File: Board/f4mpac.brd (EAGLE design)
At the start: 59.7 x 82.5 mm, 53 parts, among them CN1 DIP40 MB CONN, IC1 YM2413, IC10 27C512AL, IC2 74LS30D, IC3 74LS04D, IC4 LM4558N, IC5 Z80, IC6 74LS30D, IC7 74LS02D, IC8 74LS74D, IC9 74LS125D

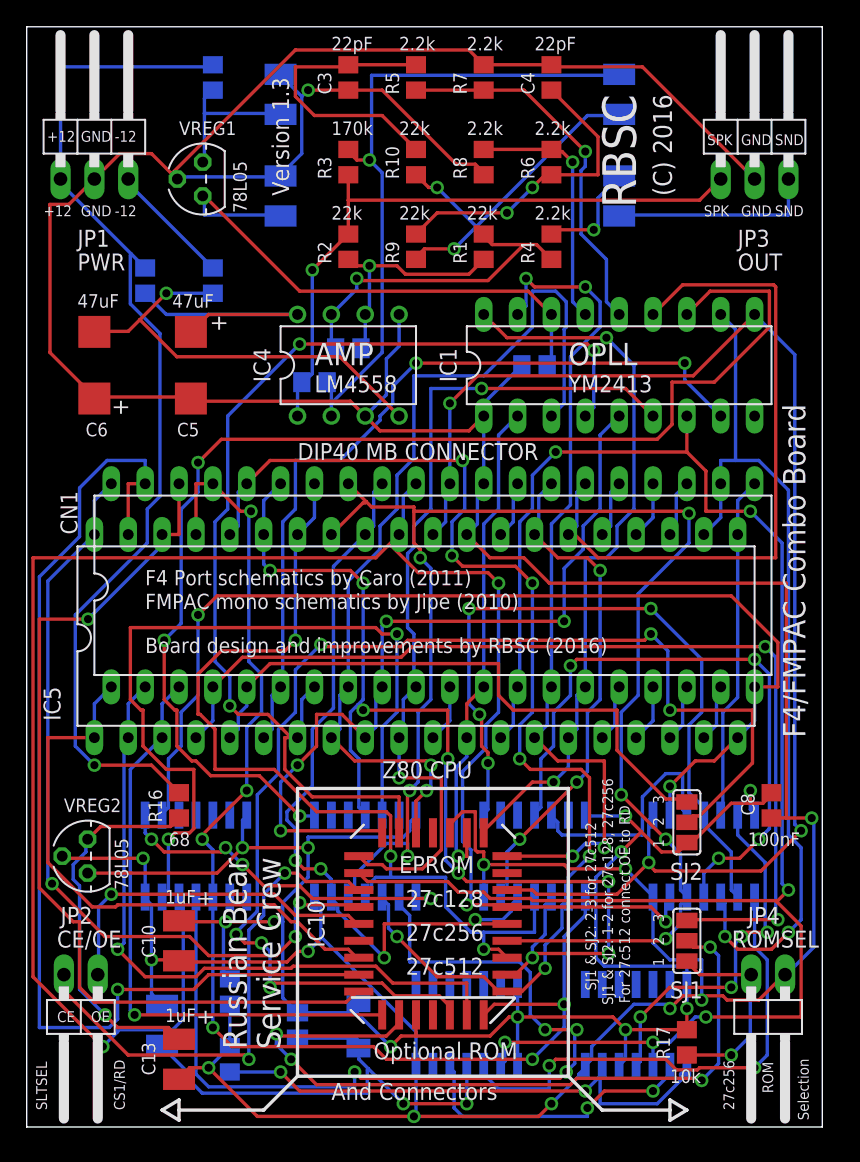
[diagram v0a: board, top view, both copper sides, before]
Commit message: Release 23.01.2019
Improved board, redrawn schematics
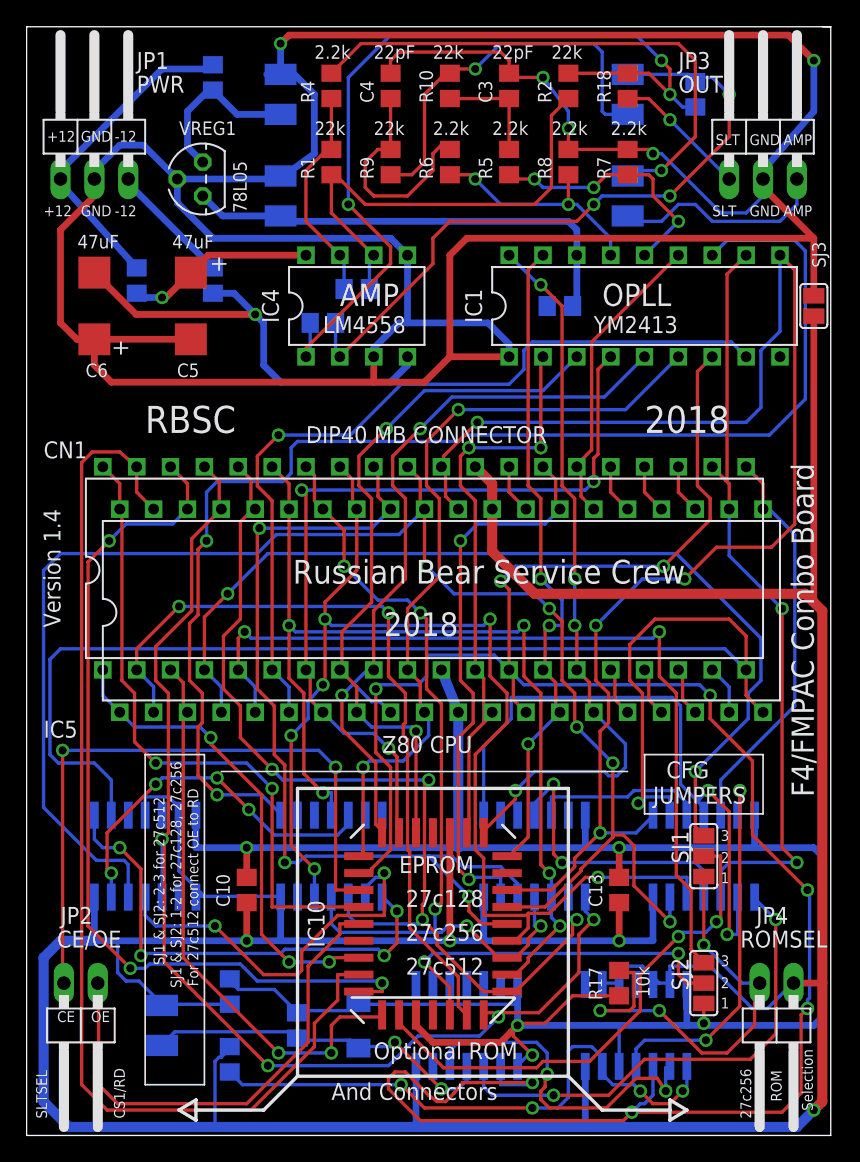
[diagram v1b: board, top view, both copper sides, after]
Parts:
- removed C15: 100nF, rcl:C0805
- removed R16: 68, rcl:R0805
- removed VREG2: 7805L, linear:TO92
- added R18: 1k, rcl:R0805
- added SJ3: (no value), jumper:SJ
- C10, C13: value 1uF 25v -> 100nF; device rcl:SMC_B -> rcl:C0805
- R4: value 2.2k -> 4.7k
- moved C8 40.7 mm to (40.0, 61.6), flipped to the bottom, turned to 180 degrees
- moved C13 35.4 mm to (44.5, 17.8)
- moved R3 26.5 mm to (50.2, 77.5), flipped to the bottom
- moved R2 20.4 mm to (40.6, 78.1)
- moved R4 20.4 mm to (22.9, 78.1)
- moved R1 13.1 mm to (22.9, 72.4)
- moved R7 12.5 mm to (45.1, 72.4)
- moved SJ2 12.1 mm to (50.8, 10.8)
- moved C3 12.1 mm to (36.2, 78.1), turned to 270 degrees
- moved C4 12.1 mm to (27.3, 78.1)
- moved R5 9.44 mm to (36.2, 72.4)
- moved R6 7.62 mm to (31.8, 72.4), turned to 90 degrees
- moved R17 6.75 mm to (44.5, 10.8), turned to 90 degrees
- moved R9 6.63 mm to (27.3, 72.4)
- moved SJ1 6.48 mm to (50.8, 20.3)
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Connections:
- net N$2 renamed AMP
- net N$5 renamed +12VAMP
- net N$8 renamed -12VAMP
- removed net N$22 (its old number): C13.+, R16.1, VREG2.3
- removed net N$23: C12.+, C15.2, IC1.16, VREG1.1
- removed net VCC: CN1.11, IC5.11
- new net +5V: C10.1, C11.1, C13.1, CN1.11, D1.C, IC10.32, IC2.14, IC3.14, IC5.11, IC6.14, IC7.14, IC8.1, IC8.14, IC9.14, IC9.5, R15.1, R17.1, SJ2.1
- new net SLT: JP3.1, R18.2
- net +12V: no longer R16.2
- net +5VREG: now also C12.+, IC1.16, VREG1.1; no longer C10.+, C11.1, D1.C, IC10.32, IC2.14, IC3.14, IC6.14, IC7.14, IC8.1, IC8.14, IC9.14, IC9.5, R15.1, R17.1, SJ2.1, VREG2.1
- net GND: now also C10.2, C13.2, IC3.1, IC3.11, IC3.13, IC9.10, IC9.12, IC9.13, IC9.9, SJ3.1, SJ3.2; no longer C10.-, C13.-, C15.1, VREG2.2
- net N$40: now also R18.1; no longer JP3.1
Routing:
- net GND: track 370.6 -> 568.7 mm, vias 12 -> 9
- net +5V: track 0.00 -> 168.0 mm, vias 0 -> 5
- net +5VREG: track 141.8 -> 34.9 mm, vias 11 -> 0
- net N$25: track 93.6 -> 27.8 mm, vias 6 -> 2
- net +12V: track 79.0 -> 24.2 mm, vias 1 -> 0
- net N$23: track 41.1 -> 0.00 mm
- net N$17: track 68.2 -> 29.6 mm, vias 4 -> 2
- net N$11: track 8.14 -> 40.8 mm
- net N$15: track 59.4 -> 27.6 mm, vias 2 -> 4
- net D7: track 143.3 -> 173.0 mm, vias 6 -> 8
- net N$22 (its old number): track 28.6 -> 0.00 mm, vias 1 -> 0
- net RST: track 51.1 -> 22.8 mm
- net N$24: track 47.6 -> 21.9 mm, vias 4 -> 2
- net A1: track 141.0 -> 117.3 mm, vias 4 -> 5
- net IORQ: track 79.9 -> 101.1 mm, vias 2 -> 1
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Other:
- board size 59.7 x 82.5 mm -> 60.3 x 83.2 mm
- board text added: "(C) 2018"
- board text added: "2018"
- board text added: "Board design and improvements by RBSC (2018)"
- board text added: "CFG JUMPERS"
- board text added: "Russian Bear Service Crew"
- board text added: "SLT"
- board text added: "Version 1.4"
- board text removed: "(C) 2016"
- board text removed: "Board design and improvements by RBSC (2016)"
- board text removed: "C10"
- board text removed: "C13"
- board text removed: "C15"
- board text removed: "R16"
- board text removed: "SND"
- board text removed: "SPK"
- board text removed: "VREG2"
- board text removed: "Version 1.3"
